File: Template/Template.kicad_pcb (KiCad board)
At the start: 2 copper layers, 32 parts, among them J1 CAN, J2 CAN, J3 SWD_UART, SW1 DBG2, SW2 DBG1, SW3 RST, U1 STM32F072CBUx, U2 AZ1117-3.3, U3 ATA6561

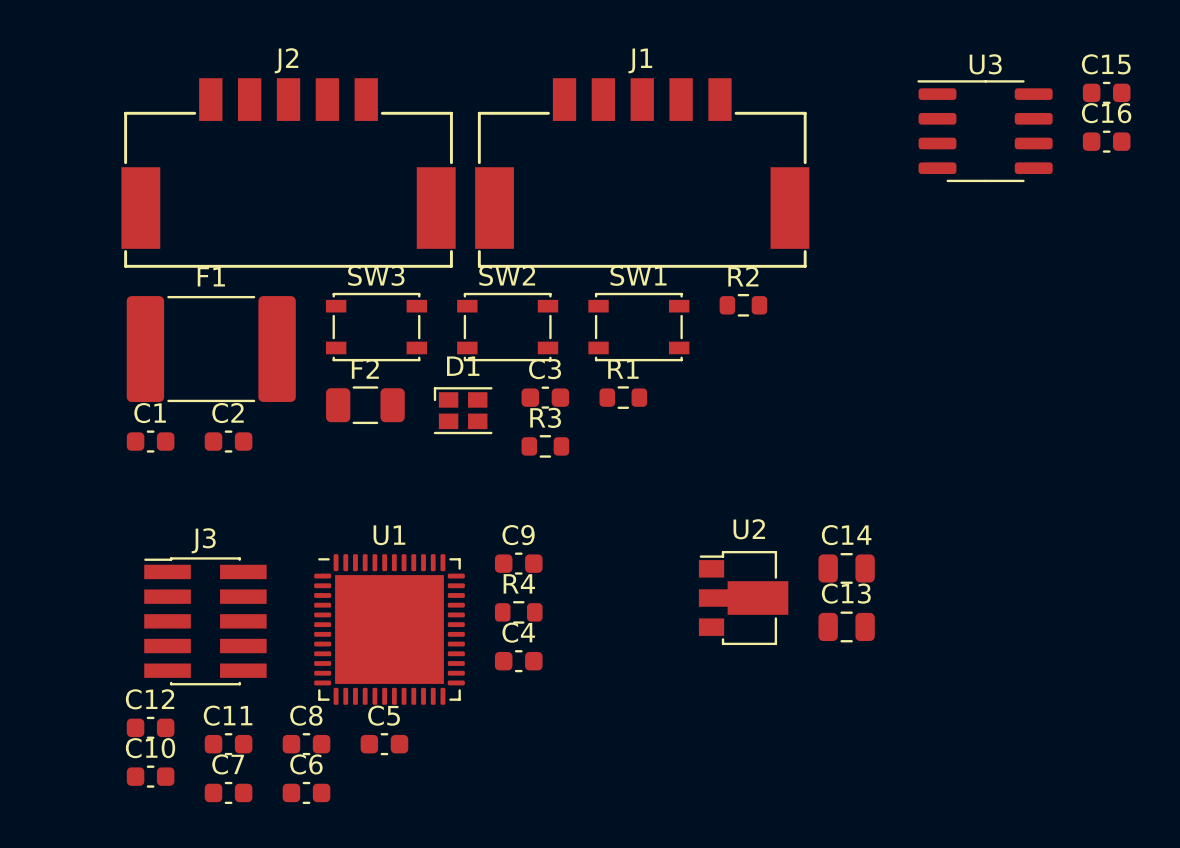
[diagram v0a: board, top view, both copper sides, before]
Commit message: Updated Template to use 3D models
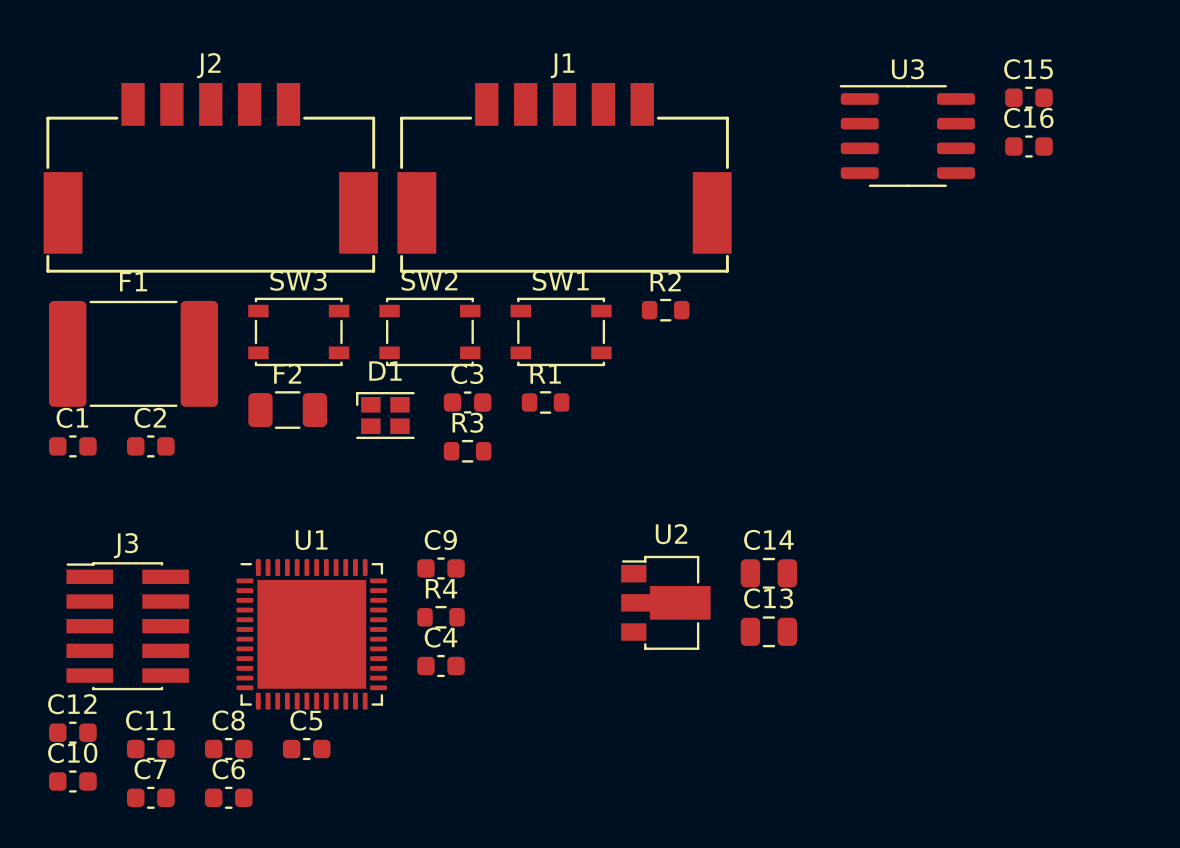
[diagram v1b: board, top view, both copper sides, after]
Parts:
- moved C1 4.01 mm to (120.0, 101.5)
- moved C10 4.01 mm to (120.0, 118.7)
- moved C12 4.01 mm to (120.0, 116.2)
- moved C13 4.01 mm to (155.8, 111.0)
- moved C14 4.01 mm to (155.8, 108.0)
- moved C15 4.01 mm to (169.2, 83.6)
- moved C16 4.01 mm to (169.2, 86.1)
- moved C3 4.01 mm to (140.3, 99.2)
- moved C4 4.01 mm to (138.9, 112.8)
- moved C5 4.01 mm to (132.0, 117.1)
- moved C6 4.01 mm to (128.0, 119.6)
- moved C8 4.01 mm to (128.0, 117.1)
- moved C9 4.01 mm to (138.9, 107.8)
- moved D1 4.01 mm to (136.1, 99.9)
- moved F1 4.01 mm to (123.1, 96.7)
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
